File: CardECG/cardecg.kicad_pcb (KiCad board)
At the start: 2 copper layers, 56 parts, among them CN1 2TAP, P1 PROG, P2 BATTERY, P3 FORCE ON, Q1 BSS84P, Q2 NTR1P02T1, Q3 BSS84P, Q4 NTR1P02T1, Q5 NMOS_GSD, Q6 NMOS_GSD, Q7 NTR1P02T1, U1 LMV341, U2 TPS717, U3 ADuC7061, U4 SSD1306, U5 creditcard, U6 DNP, U7 DNP

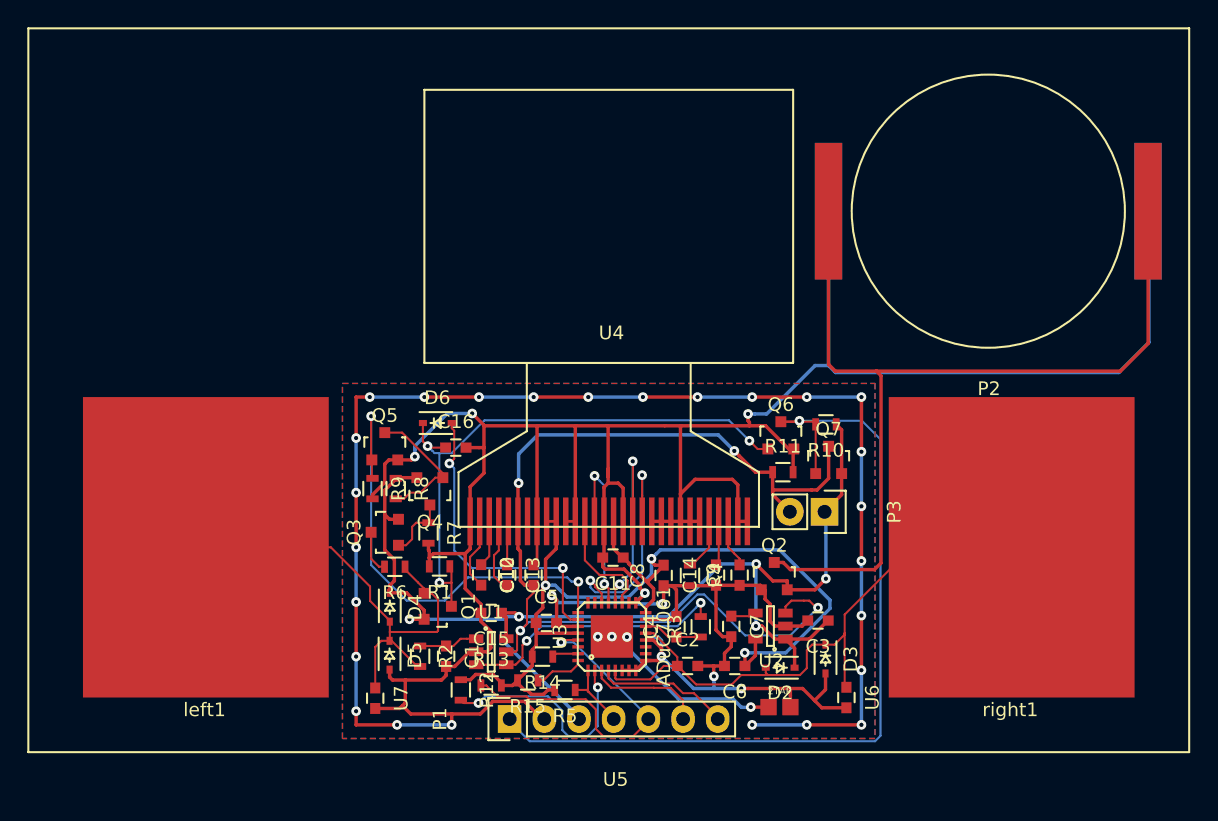
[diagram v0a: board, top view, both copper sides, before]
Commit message: Moved the components a little bit upward.
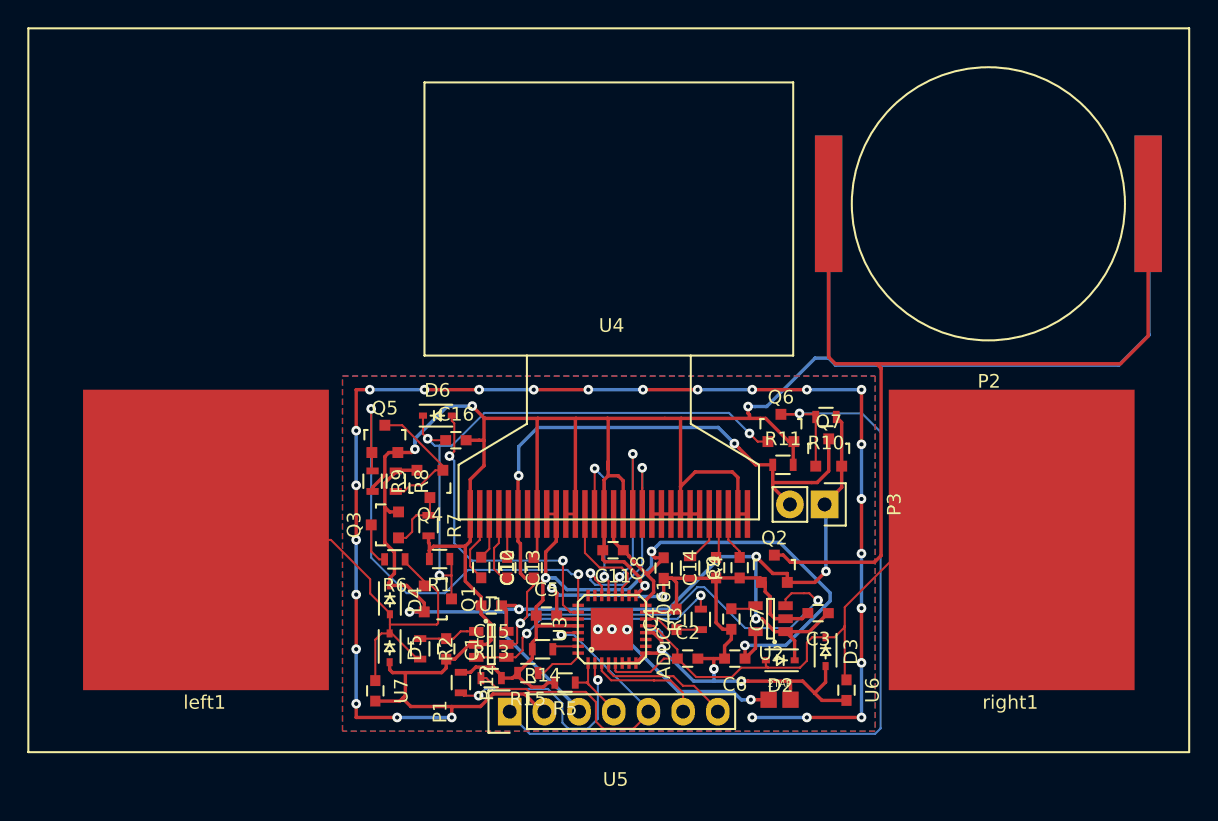
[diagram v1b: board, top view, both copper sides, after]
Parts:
- moved C1 0.54 mm to (56.6, 69.4)
- moved C15 0.54 mm to (59.9, 66.3)
- moved C5 0.54 mm to (63.9, 67.0)
- moved C8 0.54 mm to (72.5, 63.5)
- moved CN1 0.54 mm to (81.0, 73.2)
- moved D2 0.54 mm to (81.1, 70.3)
- moved D5 0.54 mm to (52.5, 69.4)
- moved P2 0.54 mm to (96.3, 36.8)
- moved Q1 0.54 mm to (56.0, 65.8)
- moved R14 0.54 mm to (63.7, 69.5)
- moved R2 0.54 mm to (54.7, 69.4)
- moved R4 0.54 mm to (74.5, 63.5)
- moved R5 0.54 mm to (65.3, 71.9)
- moved U2 0.54 mm to (80.3, 67.2)
- moved U3 0.54 mm to (68.7, 68.0)
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
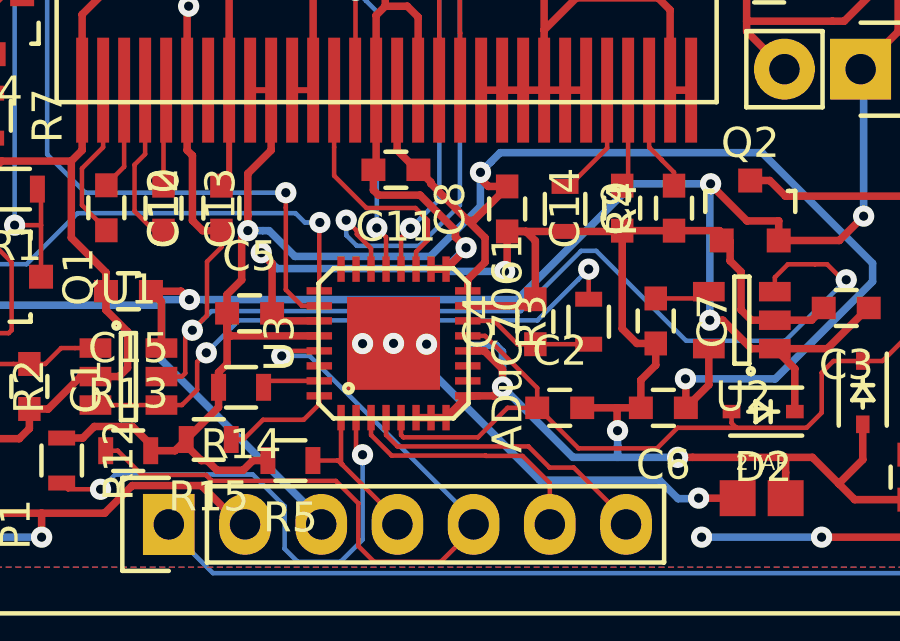
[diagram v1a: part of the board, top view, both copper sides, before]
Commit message: Added 1uF capacitor to AVDD
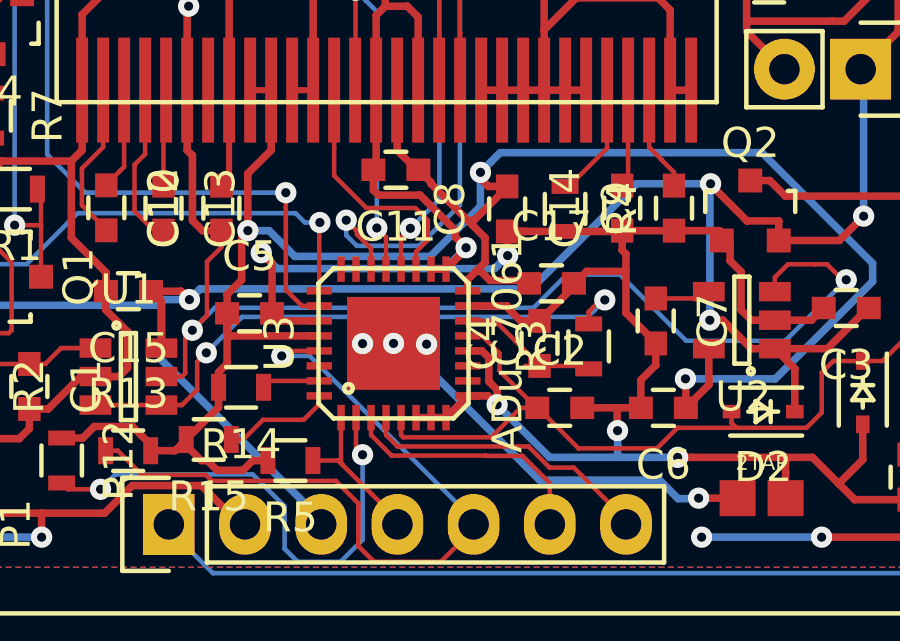
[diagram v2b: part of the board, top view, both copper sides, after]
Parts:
- added C17: 1uF, Capacitors_SMD:C_0603, F.Cu at (74.0, 66.0)
- moved R3 0.82 mm to (75.2, 68.1)
- moved C4 0.74 mm to (73.6, 68.0)
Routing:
- net VDD: track 73.0 -> 74.9 mm
- net GND: track 367.8 -> 366.5 mm
- net Net-(C4-Pad1): track 4.35 -> 5.19 mm
- net VCC: track 75.3 -> 74.7 mm
